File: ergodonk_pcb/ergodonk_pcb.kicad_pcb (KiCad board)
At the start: 2 copper layers, 184 x 152.6 mm, 116 parts, among them J1 AudioJack4, Q1 TIP120

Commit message: LH single side pcb first draft complete sent this version to jlcpcb for prototype production
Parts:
- removed REF**: uxcell a14092600ux0438 solenoid, ergodonk_kicad_library:uxcell a14092600ux0438 solenoid
- added H10: MountingHole, MountingHole:MountingHole_2.2mm_M2_Pad_Via, F.Cu at (91.5, 95.5)
- added JP1: SolderJumper_3_Open, Keebio-Parts:SolderJumper, F.Cu at (57.9, 60.4)
- added U1: Solenoid, ergodonk_kicad_library:uxcell a14092600ux0438 solenoid, B.Cu at (143.7, 49.9)
- added U2: Pico, MCU_RaspberryPi_and_Boards:RPi_Pico_SMD_TH, F.Cu at (255.9, 45.7)
- D1, D11, D12, D13, D14, D15, D16, D17, D18, D2, D21, D22, D23, D24, D25, D26, D27, D28, D3, D31, D32, D33, D34, D35, D36, D37, D38, D4, D41, D42, D43, D44, D45, D46, D47, D48, D5, D50, D51, D52, D53, D54, D56, D57, D58, D6, D65, D68, D7, D_SOL_1, J_SOL_1, Q1, R2: moved to B.Cu
- H1, H2, H3, H4, H5, H6, H7, H8, H9: footprint MountingHole:MountingHole_3.2mm_M3_Pad_Via -> MountingHole:MountingHole_2.2mm_M2_Pad_Via
- H10: footprint MountingHole:MountingHole_3.2mm_M3_Pad_Via -> ergodonk_kicad_library:MountingHole_2.05mm_M2_Pad_Via
- J1: footprint kbd:MJ-4PP-9_1side -> kbd:MJ-4PP-9
- moved H8 47.8 mm to (49.1, 101.6)
- moved H7 37.9 mm to (42.8, 139.8)
- moved H4 31.4 mm to (179.2, 156.5)
- moved H9 28.2 mm to (58.7, 44.4)
- moved H2 26.5 mm to (176.7, 51.8)
- moved H3 23.2 mm to (182.4, 93.6)
- moved R1 15.3 mm to (190.1, 56.8), turned to 0 degrees
- moved D47 13.4 mm to (182.0, 119.5), turned to -90 degrees
- moved H10 11.6 mm to (137.2, 91.4)
- moved H1 10.7 mm to (117.7, 48.4)
- moved SWLH_ROT1 7.53 mm to (165.6, 128.2), turned to 0 degrees
- moved D68 6.73 mm to (177.9, 168.4)
- moved Q1 5.06 mm to (68.2, 54.1), turned to 90 degrees
- moved R2 3.29 mm to (67.4, 44.1)
- moved D3 1.83 mm to (89.5, 46.1)
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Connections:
- net Net-(R2-Pad2) renamed SOLENOID_CONTROL
- J1 pad A: (no net) -> GND
- J1 pad B: (no net) -> TRRS_VCC
- J1 pad C: (no net) -> Net-(J1-PadC)
- J1 pad D: (no net) -> unconnected-(J1-PadD)
- Q1 pad 3: SOL_GND -> GND
- R1 pad 1: Net-(J1-PadR2) -> Net-(J1-PadC)
- SWLH_ROT1 pad C: SOL_GND -> GND
- ULH1 pad 18: SOL_VCC -> TRRS_VCC
- ULH1 pad 19: SOL_GND -> GND
- ULH1 pad 34: HAND -> Net-(JP1-Pad2)
- ULH1 pad 38: HAND -> Net-(JP1-Pad1)
- ULH1 pad 39: SOL_GND -> GND
- ULH1 pad 41: SOL_GND -> GND
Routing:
- net TRRS_VCC: track 0.00 -> 127.9 mm, vias 0 -> 1
- net encA: track 0.00 -> 120.4 mm, vias 0 -> 1
- net encB: track 0.00 -> 115.4 mm, vias 0 -> 1
- net TRRS1: track 0.00 -> 108.5 mm
- net col6: track 110.7 -> 190.7 mm, vias 0 -> 2
- net SW47A: track 157.5 -> 233.6 mm, vias 1 -> 2
- net Net-(JP1-Pad1): track 0.00 -> 54.1 mm, vias 0 -> 1
- net row4: track 208.3 -> 254.6 mm
- net Net-(JP1-Pad2): track 0.00 -> 44.2 mm
- net SW47B: track 0.00 -> 34.3 mm, vias 0 -> 1
- net SOL_VCC: track 6.61 -> 29.1 mm, vias 0 -> 1
- net Net-(J1-PadC): track 0.00 -> 15.4 mm
- net row5: track 256.3 -> 265.2 mm
- net Net-(Q1-Pad1): track 5.92 -> 13.2 mm
- net unconnected-(J1-PadD): track 0.00 -> 7.00 mm
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- added copper zone on B.Cu, net GND

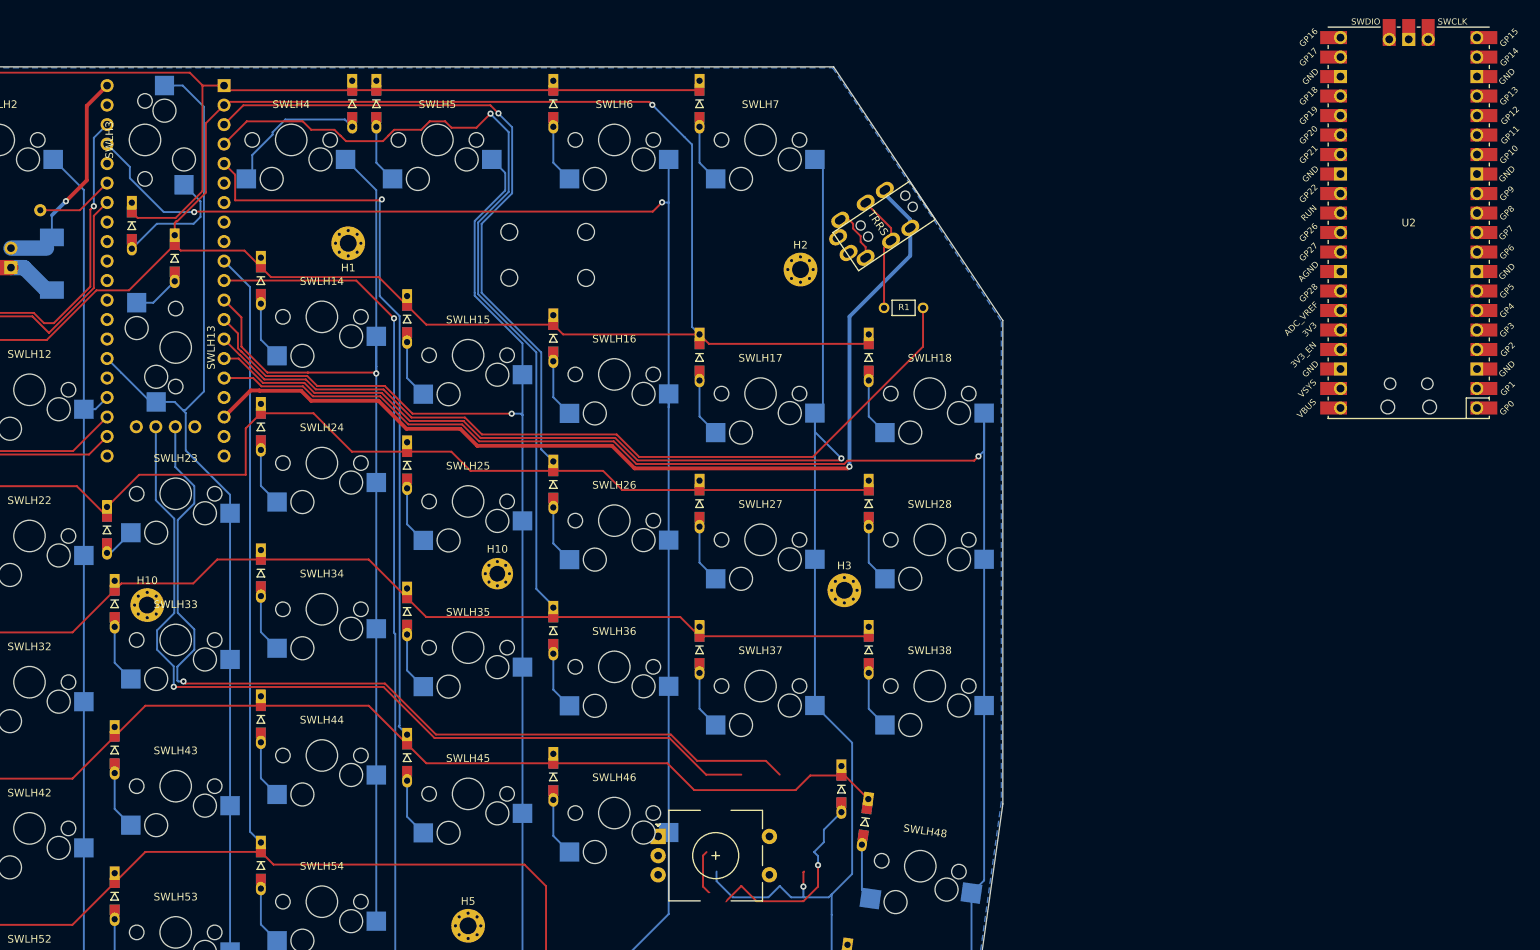
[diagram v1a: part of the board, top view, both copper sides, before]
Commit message: Synchronized updated footprints with schematics
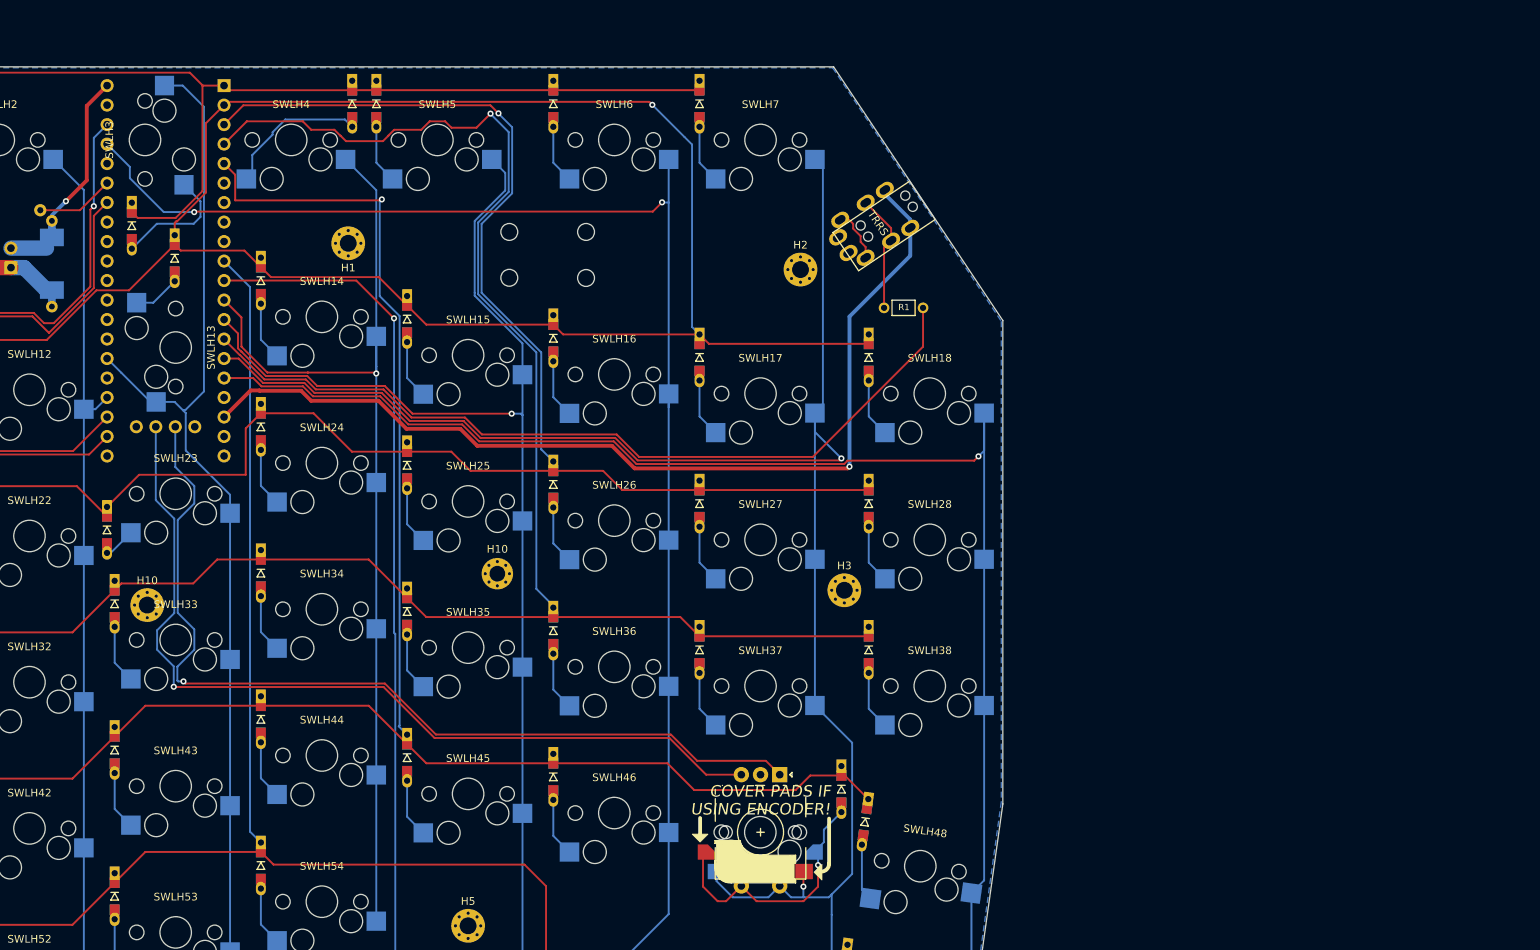
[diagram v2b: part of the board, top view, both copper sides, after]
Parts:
- removed U2: Pico, MCU_RaspberryPi_and_Boards:RPi_Pico_SMD_TH
- D_SOL_1: footprint MUR340S:DIOM6859X262N -> Neffs_kicad_footprint_library:MUR340S_IN4004_TH
- SWLH_ROT1: footprint Keebio-Parts:RotaryEncoder_EC11 -> ergodonk_kicad_library:RotaryEncoder_EC11_with_MX_hotswap_v2

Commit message: Added 2u Screw in stabalizers and rerouted wiring
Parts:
- added J2: ICSP, Keebio-Parts:Header-12-Pin-ZigZag-Square, F.Cu at (251.7, 98.8)
- added Low Profile Hybrid: MXLP/Choc, Keebio-Parts:Low-Profile-Choc-MX, F.Cu at (272.0, 129.7)
- added REF*: I2C_Breakout, Keebio-Parts:I2C_Breakout, F.Cu at (266.7, 104.6)
- added REF**: RPi_Pico_SMD_TH, MCU_RaspberryPi_and_Boards:RPi_Pico_SMD_TH, F.Cu at (245.4, 47.8)
- added U1: ProMicro-18mil-offset, Keebio-Parts:ArduinoProMicro-ZigZag, F.Cu at (281.2, 37.0)
- added U1: ProMicro, Keebio-Parts:ArduinoProMicro, F.Cu at (281.3, 74.7)
- SWLH1, SWLH11, SWLH12, SWLH13, SWLH14, SWLH15, SWLH16, SWLH17, SWLH18, SWLH2, SWLH22, SWLH23, SWLH24, SWLH25, SWLH26, SWLH27, SWLH28, SWLH3, SWLH32, SWLH33, SWLH34, SWLH35, SWLH36, SWLH37, SWLH38, SWLH4, SWLH42, SWLH43, SWLH44, SWLH45, SWLH46, SWLH48, SWLH5, SWLH52, SWLH53, SWLH54, SWLH58, SWLH6, SWLH68, SWLH7: footprint kbd:CherryMX_Hotswap -> ergodonk_kicad_library:CherryMX_Hotswap
- SWLH21: footprint kbd:CherryMX_Hotswap_1.5u -> ergodonk_kicad_library:CherryMX_Hotswap_1.5u
- SWLH31: footprint kbd:CherryMX_Hotswap_1.75u_ergodonk -> ergodonk_kicad_library:CherryMX_Hotswap_1.75u_ergodonk
- SWLH41, SWLH56, SWLH57: footprint kbd:CherryMX_Hotswap_2u_ergodonk -> ergodonk_kicad_library:CherryMX_Hotswap_2u_ergodonk_Stabs
- SWLH50, SWLH51: footprint kbd:CherryMX_Hotswap_1.25u_ergodonk -> ergodonk_kicad_library:CherryMX_Hotswap_1.25u_ergodonk
- SWLH65: footprint kbd:CherryMX_Hotswap_1.25u_Vert_ergodonk -> ergodonk_kicad_library:CherryMX_Hotswap_1.25u_Vert_ergodonk
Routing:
- net row5: track 265.2 -> 259.3 mm
- net row4: track 254.6 -> 255.4 mm

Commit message: Wiring cleanup, started adding LEDs
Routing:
- net row4: track 255.4 -> 270.6 mm
- net row2: track 246.4 -> 258.6 mm
- net row0: track 148.4 -> 154.5 mm
- net col5: track 174.4 -> 177.9 mm
- net Net-(JP1-Pad1): track 54.1 -> 51.8 mm
- net Net-(JP1-Pad2): track 44.2 -> 42.5 mm
- net encA: track 120.4 -> 119.4 mm
- net encB: track 115.4 -> 114.8 mm
